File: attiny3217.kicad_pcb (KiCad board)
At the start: 2 copper layers, 19.3 x 34.6 mm, 12 parts, among them J1 Conn_01x12_Male, J2 Conn_01x12_Male, J3 Conn_01x03_Male, SW1 SW_Push, U1 ATtiny3217-M

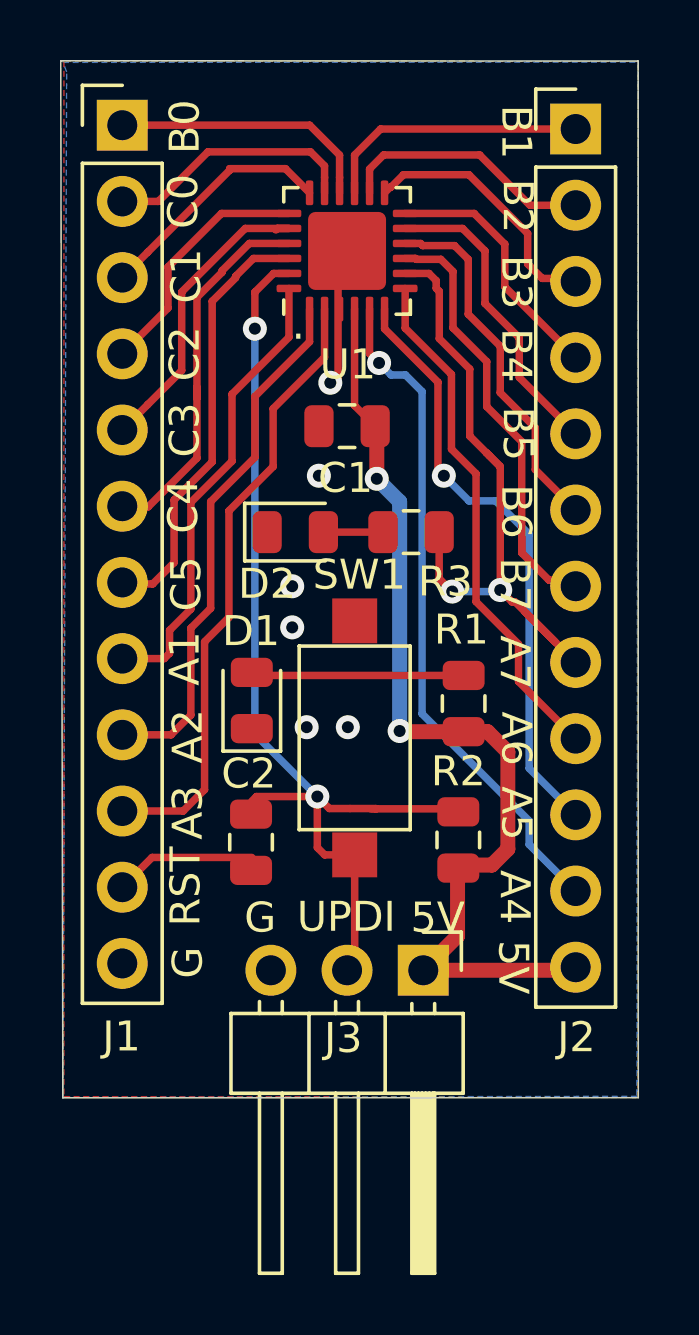
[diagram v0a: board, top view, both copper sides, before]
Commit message: consolidate files from two directories
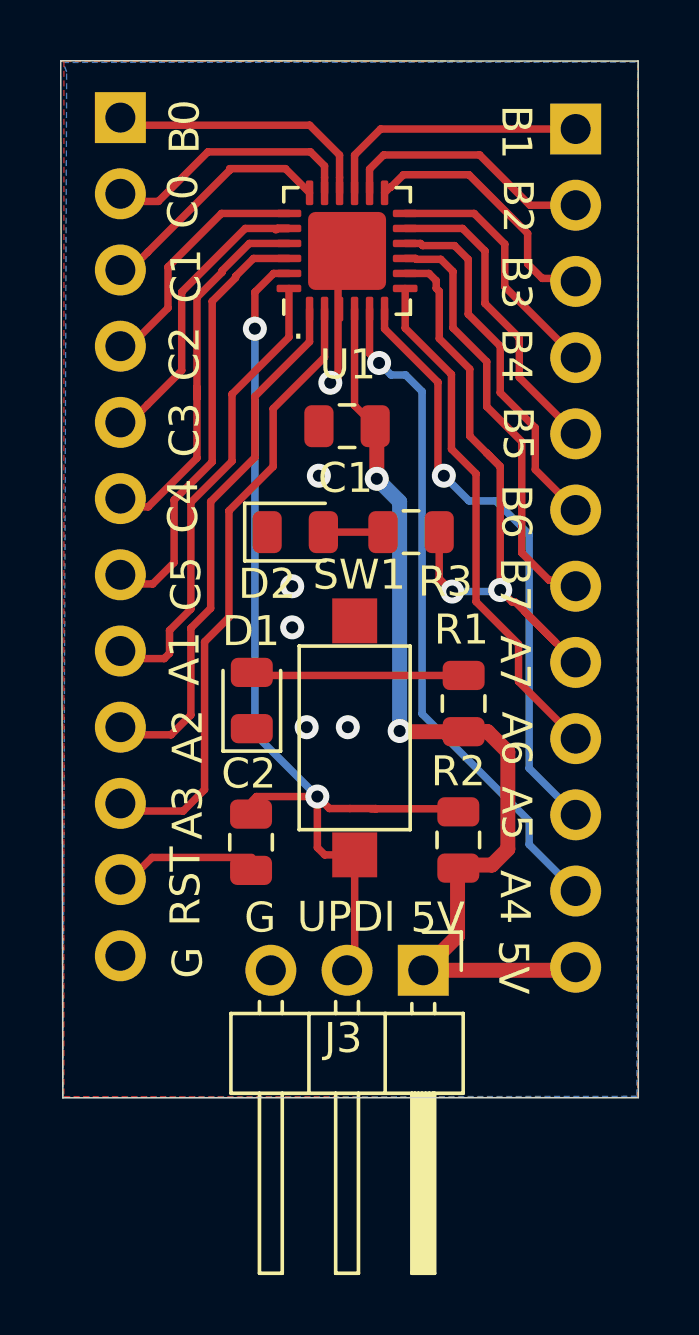
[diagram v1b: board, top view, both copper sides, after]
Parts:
- J1, J2: moved to B.Cu
- moved J1 0.26 mm to (127.0, 65.8), turned to 180 degrees
- turned J2 to 180 degrees
